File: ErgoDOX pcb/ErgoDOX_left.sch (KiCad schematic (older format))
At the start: 105 parts, among them J1 AudioJack4, J2 USB_B_Micro, SW0:10 SW0:3, SW0:11 SW0:2, SW0:12 SW0:1, SW0:7 SW0:6, SW0:8 SW0:5, SW0:9 SW0:4, SW1 TS-1187A-B-A-B, SW1:10 SW1:3, SW1:11 SW1:2, SW1:12 SW1:1, SW1:13 SW1:0, SW1:9 SW1:4, SW2:10 SW2:3, SW2:11 SW2:2, SW2:12 SW2:1, SW2:13 SW2:0, SW2:7 SW2:6, SW2:8 SW2:5, SW2:9 SW2:4, SW3:10 SW3:3, SW3:11 SW3:2, SW3:12 SW3:1, SW3:13 SW3:0, SW3:8 SW3:5, SW3:9 SW3:4, SW4:10 SW4:3, SW4:11 SW4:2, SW4:12 SW4:1, SW4:13 SW4:0, SW4:7 SW4:6, SW4:8 SW4:5, SW4:9 SW4:4, SW5:10 SW5:3, SW5:11 SW5:2, SW5:12 SW5:1, SW5:13 SW5:0, SW5:7 SW5:6, SW5:8 SW5:5, SW5:9 SW5:4, U1 ATmega32U4-MU, U2 MCP23018, Y1 16MHz

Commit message: finished LH routing
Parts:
- removed R6, R7: 1k, Resistors_SMD:R_0603, symbol Device:R_US
- removed U2: MCP23018, Housings_SSOP:SSOP-24_5.3x8.2mm_Pitch0.65mm, symbol ErgoDOX:MCP23018
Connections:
- no-connect marks 12 -> 6
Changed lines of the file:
@@
 	1    0    0    -1
 $EndComp
-Text Label 14400 4200 0    60   ~ 0
-COL1
 Text Label 13300 1450 2    60   ~ 0
 LED_A
@@
 	1    0    0    -1
 $EndComp
-Text Label 14400 5100 0    60   ~ 0
-ROW4
-Text Label 14400 5200 0    60   ~ 0
-ROW3
-Text Label 14400 5300 0    60   ~ 0
-ROW2
-Text Label 14400 5400 0    60   ~ 0
-ROW1
-Text Label 14400 5500 0    60   ~ 0
-ROW0
-Text Label 14400 4700 0    60   ~ 0
-COL6
-Text Label 14400 4600 0    60   ~ 0
-COL5
-Text Label 14400 4100 0    60   ~ 0
-COL0
-Text Label 14400 4300 0    60   ~ 0
-COL2
-Text Label 14400 4400 0    60   ~ 0
-COL3
-Text Label 14400 4500 0    60   ~ 0
-COL4
-Text Label 12400 4350 0    60   ~ 0
-SCL
-Text Label 12400 4450 0    60   ~ 0
-SDA
-NoConn ~ 12800 5500
-NoConn ~ 12800 4950
-NoConn ~ 12800 4850
 $Comp
 L ErgoDOX:SWITCH_PUSH SW2:10
@@
 	1    0    0    -1
 $EndComp
-Text Label 14400 5000 0    60   ~ 0
-ROW5
 Text Label 1300 5800 2    60   ~ 0
 ROW5
@@
 	1    0    0    -1
 $EndComp
-NoConn ~ 14400 4800
 $Comp
 L ErgoDOX:SWITCH_PUSH SW1:9
@@
 	1    0    0    -1
 $EndComp
-NoConn ~ 12800 5600
-NoConn ~ 12800 5700
 Text Label 5200 9550 3    60   ~ 0
 COL12
@@
 Wire Wire Line
 	2200 6900 2200 6700
-Wire Wire Line
-	12350 4200 12350 4350
-Wire Wire Line
-	12250 4200 12250 4450
 Connection ~ 2300 8400
 Wire Wire Line
@@
 Connection ~ 4400 9050
 Connection ~ 3000 9050
-Text Label 14400 5600 0    60   ~ 0
-LED_B
-Text Label 14400 5700 0    60   ~ 0
-LED_A
 Wire Wire Line
 	2300 8400 3000 8400
@@
 $EndComp
 $Comp
-L Device:R_US R7
-U 1 1 5F7D2D04
-P 12350 4050
-F 0 "R7" H 12418 4096 50  0000 L CNN
-F 1 "1k" H 12418 4005 50  0000 L CNN
-F 2 "Resistors_SMD:R_0603" V 12390 4040 50  0001 C CNN
-F 3 "~" H 12350 4050 50  0001 C CNN
-	1    12350 4050
-	1    0    0    -1
-$EndComp
-$Comp
-L Device:R_US R6
-U 1 1 5F7D30B0
-P 12250 4050
-F 0 "R6" H 12182 4004 50  0000 R CNN
-F 1 "1k" H 12182 4095 50  0000 R CNN
-F 2 "Resistors_SMD:R_0603" V 12290 4040 50  0001 C CNN
-F 3 "~" H 12250 4050 50  0001 C CNN
-	1    12250 4050
-	1    0    0    1
-$EndComp
-$Comp
-L power:VCC #PWR0110
-U 1 1 5F7D3AAF
-P 12300 3900
-F 0 "#PWR0110" H 12300 3750 50  0001 C CNN
-F 1 "VCC" H 12315 4073 50  0000 C CNN
-F 2 "" H 12300 3900 50  0001 C CNN
-F 3 "" H 12300 3900 50  0001 C CNN
-	1    12300 3900
-	1    0    0    -1
-$EndComp
-Wire Wire Line
-	12250 3900 12300 3900
-Connection ~ 12300 3900
-Wire Wire Line
-	12300 3900 12350 3900
-$Comp
 L power:GND #PWR0111
 U 1 1 5F7E762D
@@
 Wire Wire Line
 	14000 3100 13950 3100
-$Comp
-L power:GND #PWR0114
-U 1 1 5F857BF3
-P 12800 4650
-F 0 "#PWR0114" H 12800 4400 50  0001 C CNN
-F 1 "GND" V 12805 4522 50  0000 R CNN
-F 2 "" H 12800 4650 50  0001 C CNN
-F 3 "" H 12800 4650 50  0001 C CNN
-	1    12800 4650
-	0    1    1    0
-$EndComp
-$Comp
-L power:VCC #PWR0115
-U 1 1 5F858643
-P 12800 4100
-F 0 "#PWR0115" H 12800 3950 50  0001 C CNN
-F 1 "VCC" H 12815 4273 50  0000 C CNN
-F 2 "" H 12800 4100 50  0001 C CNN
-F 3 "" H 12800 4100 50  0001 C CNN
-	1    12800 4100
-	1    0    0    -1
-$EndComp
-$Comp
-L ErgoDOX:MCP23018 U2
-U 1 1 5F78DF8E
-P 13600 4900
-F 0 "U2" H 13600 6048 60  0000 C CNN
-F 1 "MCP23018" H 13600 5942 60  0000 C CNN
-F 2 "Housings_SSOP:SSOP-24_5.3x8.2mm_Pitch0.65mm" H 13600 4900 50  0001 C CNN
-F 3 "" H 13600 4900 50  0001 C CNN
-	1    13600 4900
-	1    0    0    -1
-$EndComp
 $Comp
 L Switch:SW_Push SW1
@@
 Text Label 13450 2250 2    60   ~ 0
 SDA
-Wire Wire Line
-	12250 4450 12800 4450
-Wire Wire Line
-	12350 4350 12800 4350
 Text Label 9950 2150 2    60   ~ 0
 RST

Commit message: USB breakout draft
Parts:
- added J101: USB_C_Receptacle_USB2.0, Connectors_USB:USB_C_Receptacle_Amphenol_12401548E4-2A, symbol Connector:USB_C_Receptacle_USB2.0
- added J102: USB_B_Mini, ErgoDOX:CUI_UJ2-MABH-1-SMT, symbol Connector:USB_B_Mini
- added J2, J201, J202, J203: USB_B, ErgoDOX:usb_breakout, symbol Connector:USB_B
- J103: renamed from J2; Purchase (none) -> https://www.digikey.com/en/products/detail/amphenol-icc-fci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
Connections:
- net GND: now also J101.A1 (GND), J101.A12 (GND), J101.B1 (GND), J101.B12 (GND), J101.S1 (SHIELD), J102.5 (GND), J102.6 (Shield), J2.4 (GND), J2.5 (Shield), J201.4 (GND), J201.5 (Shield), J202.4 (GND), J202.5 (Shield), J203.4 (GND), J203.5 (Shield)
- net USB+: now also J2.3 (D+); no longer J103.3 (D+)
- net USB-: now also J2.2 (D-); no longer J103.2 (D-)
- net VCC: now also J2.1 (VBUS); no longer J103.1 (VBUS)
- new net: J101.A4 (VBUS), J101.A9 (VBUS), J101.B4 (VBUS), J101.B9 (VBUS), J201.1 (VBUS)
- new net: J101.A6 (D+), J101.B6 (D+), J201.3 (D+)
- new net: J101.A7 (D-), J101.B7 (D-), J201.2 (D-)
- new net: J102.1 (VBUS), J202.1 (VBUS)
- new net: J102.2 (D-), J202.2 (D-)
- new net: J102.3 (D+), J202.3 (D+)
- new net: J103.1 (VBUS), J203.1 (VBUS)
- new net: J103.2 (D-), J203.2 (D-)
- new net: J103.3 (D+), J203.3 (D+)
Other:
- moved on the sheet: J103
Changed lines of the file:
@@
 	10550 1750 10550 1850
 $Comp
-L Connector:USB_B_Micro J2
+L Connector:USB_B_Micro J103
 U 1 1 6007DBC8
+P 3550 4700
+F 0 "J103" H 3607 5167 50  0000 C CNN
+F 1 "USB_B_Micro" H 3607 5076 50  0000 C CNN
+F 2 "Connectors_USB:USB_Micro-B_Wuerth-629105150521" H 3700 4650 50  0001 C CNN
+F 3 "~" H 3700 4650 50  0001 C CNN
+F 4 "https://www.digikey.com/en/products/detail/amphenol-icc-fci/10118193-0001LF/2785388" H 3550 4700 50  0001 C CNN "Purchase"
+	1    3550 4700
+	1    0    0    -1
+$EndComp
+$Comp
+L Connector:USB_B_Mini J102
+U 1 1 5FA03103
+P 3550 3550
+F 0 "J102" H 3607 4017 50  0000 C CNN
+F 1 "USB_B_Mini" H 3607 3926 50  0000 C CNN
+F 2 "ErgoDOX:CUI_UJ2-MABH-1-SMT" H 3700 3500 50  0001 C CNN
+F 3 "~" H 3700 3500 50  0001 C CNN
+F 4 "https://www.digikey.com/en/products/detail/cui-devices/UJ2-MABH-1-SMT-TR/6187919" H 3550 3550 50  0001 C CNN "Purchase"
+	1    3550 3550
+	1    0    0    -1
+$EndComp
+$Comp
+L Connector:USB_B J2
+U 1 1 5FA06E9E
 P 8850 3150
 F 0 "J2" H 8907 3617 50  0000 C CNN
-F 1 "USB_B_Micro" H 8907 3526 50  0000 C CNN
-F 2 "Connectors_USB:USB_Micro-B_Wuerth-629105150521" H 9000 3100 50  0001 C CNN
-F 3 "~" H 9000 3100 50  0001 C CNN
+F 1 "USB_B" H 8907 3526 50  0000 C CNN
+F 2 "ErgoDOX:usb_breakout" H 9000 3100 50  0001 C CNN
+F 3 " ~" H 9000 3100 50  0001 C CNN
 	1    8850 3150
 	1    0    0    -1
 $EndComp
+$Comp
+L Connector:USB_B J201
+U 1 1 5FA08FDF
+P 4700 2000
+F 0 "J201" H 4470 1989 50  0000 R CNN
+F 1 "USB_B" H 4470 1898 50  0000 R CNN
+F 2 "ErgoDOX:usb_breakout" H 4850 1950 50  0001 C CNN
+F 3 " ~" H 4850 1950 50  0001 C CNN
+	1    4700 2000
+	-1   0    0    -1
+$EndComp
+$Comp
+L Connector:USB_B J202
+U 1 1 5FA09CCE
+P 4500 3550
+F 0 "J202" H 4270 3539 50  0000 R CNN
+F 1 "USB_B" H 4270 3448 50  0000 R CNN
+F 2 "ErgoDOX:usb_breakout" H 4650 3500 50  0001 C CNN
+F 3 " ~" H 4650 3500 50  0001 C CNN
+	1    4500 3550
+	-1   0    0    -1
+$EndComp
+$Comp
+L Connector:USB_B J203
+U 1 1 5FA0A566
+P 4500 4700
+F 0 "J203" H 4270 4689 50  0000 R CNN
+F 1 "USB_B" H 4270 4598 50  0000 R CNN
+F 2 "ErgoDOX:usb_breakout" H 4650 4650 50  0001 C CNN
+F 3 " ~" H 4650 4650 50  0001 C CNN
+	1    4500 4700
+	-1   0    0    -1
+$EndComp
+Wire Wire Line
+	3850 4500 4200 4500
+Wire Wire Line
+	4200 4700 3850 4700
+Wire Wire Line
+	3850 4800 4200 4800
+$Comp
+L power:GND #PWR0110
+U 1 1 5FA40674
+P 4000 5100
+F 0 "#PWR0110" H 4000 4850 50  0001 C CNN
+F 1 "GND" H 4005 4927 50  0000 C CNN
+F 2 "" H 4000 5100 50  0001 C CNN
+F 3 "" H 4000 5100 50  0001 C CNN
+	1    4000 5100
+	1    0    0    -1
+$EndComp
+Wire Wire Line
+	3450 5100 3550 5100
+Connection ~ 3550 5100
+Wire Wire Line
+	3550 5100 4000 5100
+Wire Wire Line
+	4500 5100 4600 5100
+Connection ~ 4500 5100
+Connection ~ 4000 5100
+Wire Wire Line
+	4000 5100 4500 5100
+Wire Wire Line
+	3450 3950 3550 3950
+Connection ~ 3550 3950
+Wire Wire Line
+	3550 3950 4050 3950
+Connection ~ 4500 3950
+Wire Wire Line
+	4500 3950 4600 3950
+$Comp
+L power:GND #PWR0114
+U 1 1 5FA8801B
+P 4050 3950
+F 0 "#PWR0114" H 4050 3700 50  0001 C CNN
+F 1 "GND" H 4055 3777 50  0000 C CNN
+F 2 "" H 4050 3950 50  0001 C CNN
+F 3 "" H 4050 3950 50  0001 C CNN
+	1    4050 3950
+	1    0    0    -1
+$EndComp
+Connection ~ 4050 3950
+Wire Wire Line
+	4050 3950 4500 3950
+Wire Wire Line
+	3850 3550 4200 3550
+Wire Wire Line
+	4200 3650 3850 3650
+Wire Wire Line
+	3850 3350 4200 3350
+Wire Wire Line
+	3950 2100 4050 2100
+Wire Wire Line
+	4050 2100 4050 2000
+Wire Wire Line
+	4050 2000 3950 2000
+Wire Wire Line
+	4050 2000 4400 2000
+Connection ~ 4050 2000
+Wire Wire Line
+	4400 2100 4250 2100
+Wire Wire Line
+	4250 2100 4250 1800
+Wire Wire Line
+	4250 1800 4050 1800
+Wire Wire Line
+	3950 1900 4050 1900
+Wire Wire Line
+	4050 1900 4050 1800
+Connection ~ 4050 1800
+Wire Wire Line
+	4050 1800 3950 1800
+Wire Wire Line
+	4400 1800 4400 1300
+Wire Wire Line
+	4400 1300 3950 1300
+$Comp
+L power:GND #PWR0115
+U 1 1 5FB25F7C
+P 4750 2450
+F 0 "#PWR0115" H 4750 2200 50  0001 C CNN
+F 1 "GND" H 4755 2277 50  0000 C CNN
+F 2 "" H 4750 2450 50  0001 C CNN
+F 3 "" H 4750 2450 50  0001 C CNN
+	1    4750 2450
+	1    0    0    -1
+$EndComp
+Wire Wire Line
+	4700 2400 4750 2400
+Wire Wire Line
+	4750 2450 4750 2400
+Connection ~ 4750 2400
+Wire Wire Line
+	4750 2400 4800 2400
+$Comp
+L power:GND #PWR0118
+U 1 1 5FB4F6CF
+P 3200 2850
+F 0 "#PWR0118" H 3200 2600 50  0001 C CNN
+F 1 "GND" H 3205 2677 50  0000 C CNN
+F 2 "" H 3200 2850 50  0001 C CNN
+F 3 "" H 3200 2850 50  0001 C CNN
+	1    3200 2850
+	1    0    0    -1
+$EndComp
+Wire Wire Line
+	3050 2800 3200 2800
+Wire Wire Line
+	3200 2850 3200 2800
+Connection ~ 3200 2800
+Wire Wire Line
+	3200 2800 3350 2800
+$Comp
+L Connector:USB_C_Receptacle_USB2.0 J101
+U 1 1 5FA00F68
+P 3350 1900
+F 0 "J101" H 3457 2767 50  0000 C CNN
+F 1 "USB_C_Receptacle_USB2.0" H 3457 2676 50  0000 C CNN
+F 2 "Connectors_USB:USB_C_Receptacle_Amphenol_12401548E4-2A" H 3500 1900 50  0001 C CNN
+F 3 "https://www.usb.org/sites/default/files/documents/usb_type-c.zip" H 3500 1900 50  0001 C CNN
+F 4 "https://www.digikey.com/en/products/detail/gct/USB4110-GF-A/10384547" H 3350 1900 50  0001 C CNN "Purchase"
+	1    3350 1900
+	1    0    0    -1
+$EndComp

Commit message: Updated USB footprints
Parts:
- J101: footprint Connectors_USB:USB_C_Receptacle_Amphenol_12401548E4-2A -> ErgoDOX:USB4110-GF-A
- J103: footprint Connectors_USB:USB_Micro-B_Wuerth-629105150521 -> ErgoDOX:10118193-0001LF
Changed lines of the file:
@@
 F 0 "J103" H 3607 5167 50  0000 C CNN
 F 1 "USB_B_Micro" H 3607 5076 50  0000 C CNN
-F 2 "Connectors_USB:USB_Micro-B_Wuerth-629105150521" H 3700 4650 50  0001 C CNN
+F 2 "ErgoDOX:10118193-0001LF" H 3700 4650 50  0001 C CNN
 F 3 "~" H 3700 4650 50  0001 C CNN
 F 4 "https://www.digikey.com/en/products/detail/amphenol-icc-fci/10118193-0001LF/2785388" H 3550 4700 50  0001 C CNN "Purchase"
@@
 F 0 "J101" H 3457 2767 50  0000 C CNN
 F 1 "USB_C_Receptacle_USB2.0" H 3457 2676 50  0000 C CNN
-F 2 "Connectors_USB:USB_C_Receptacle_Amphenol_12401548E4-2A" H 3500 1900 50  0001 C CNN
+F 2 "ErgoDOX:USB4110-GF-A" H 3500 1900 50  0001 C CNN
 F 3 "https://www.usb.org/sites/default/files/documents/usb_type-c.zip" H 3500 1900 50  0001 C CNN
 F 4 "https://www.digikey.com/en/products/detail/gct/USB4110-GF-A/10384547" H 3350 1900 50  0001 C CNN "Purchase"

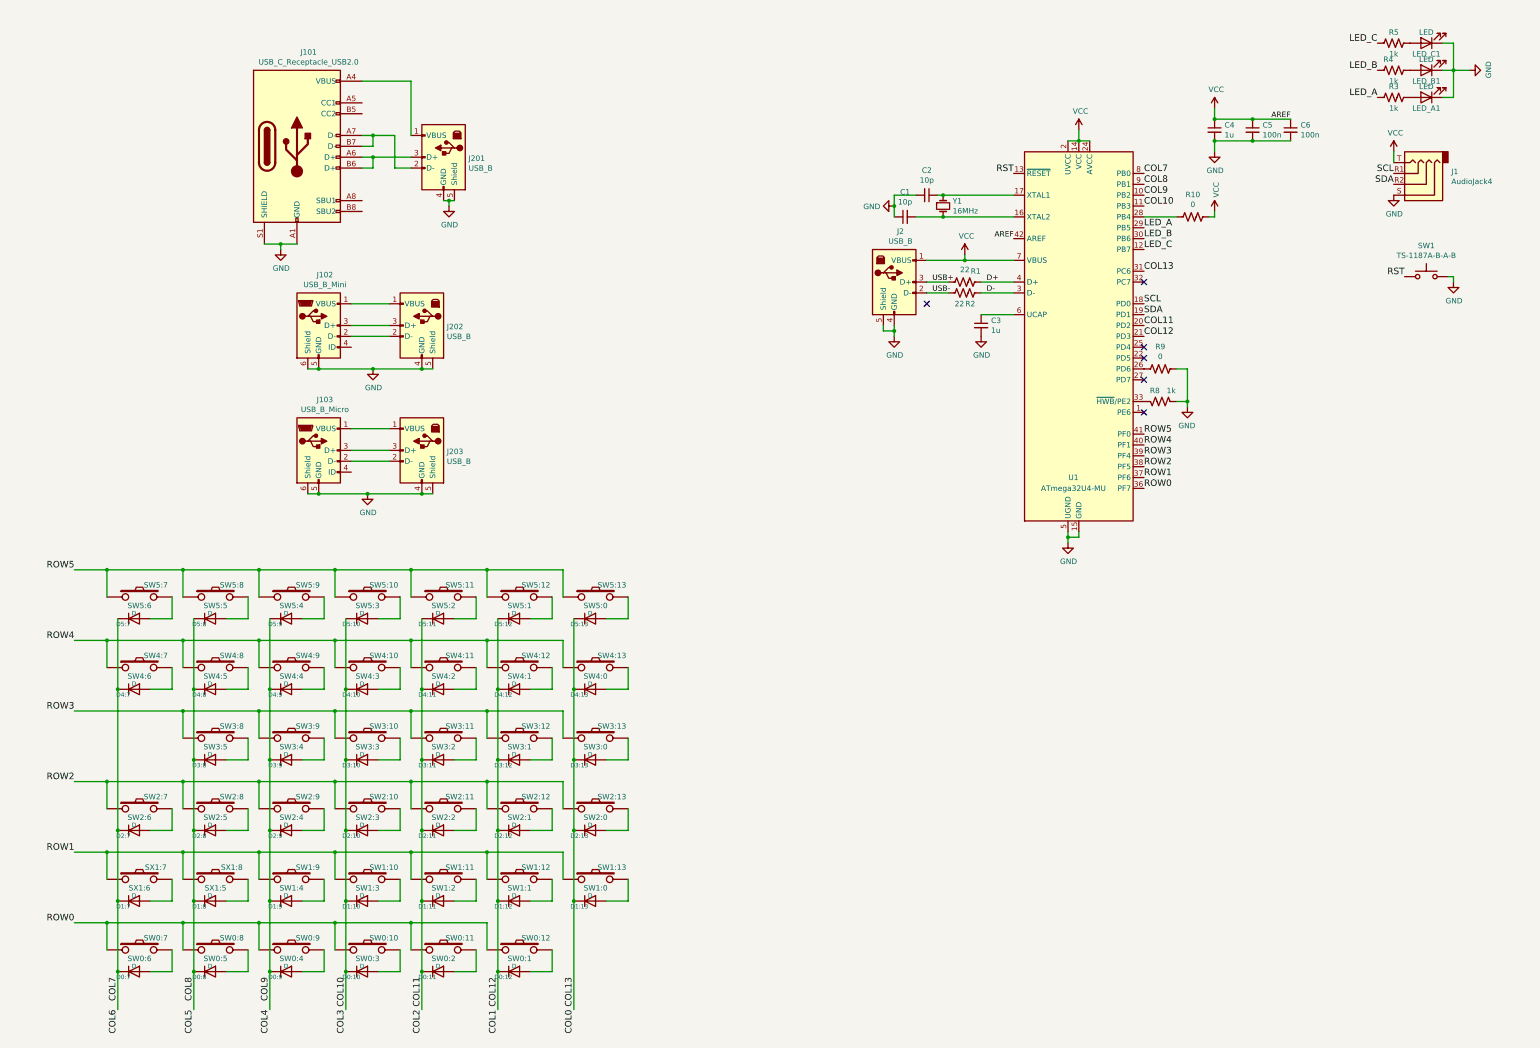
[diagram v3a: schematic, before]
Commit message: Added revision, generated gerbers
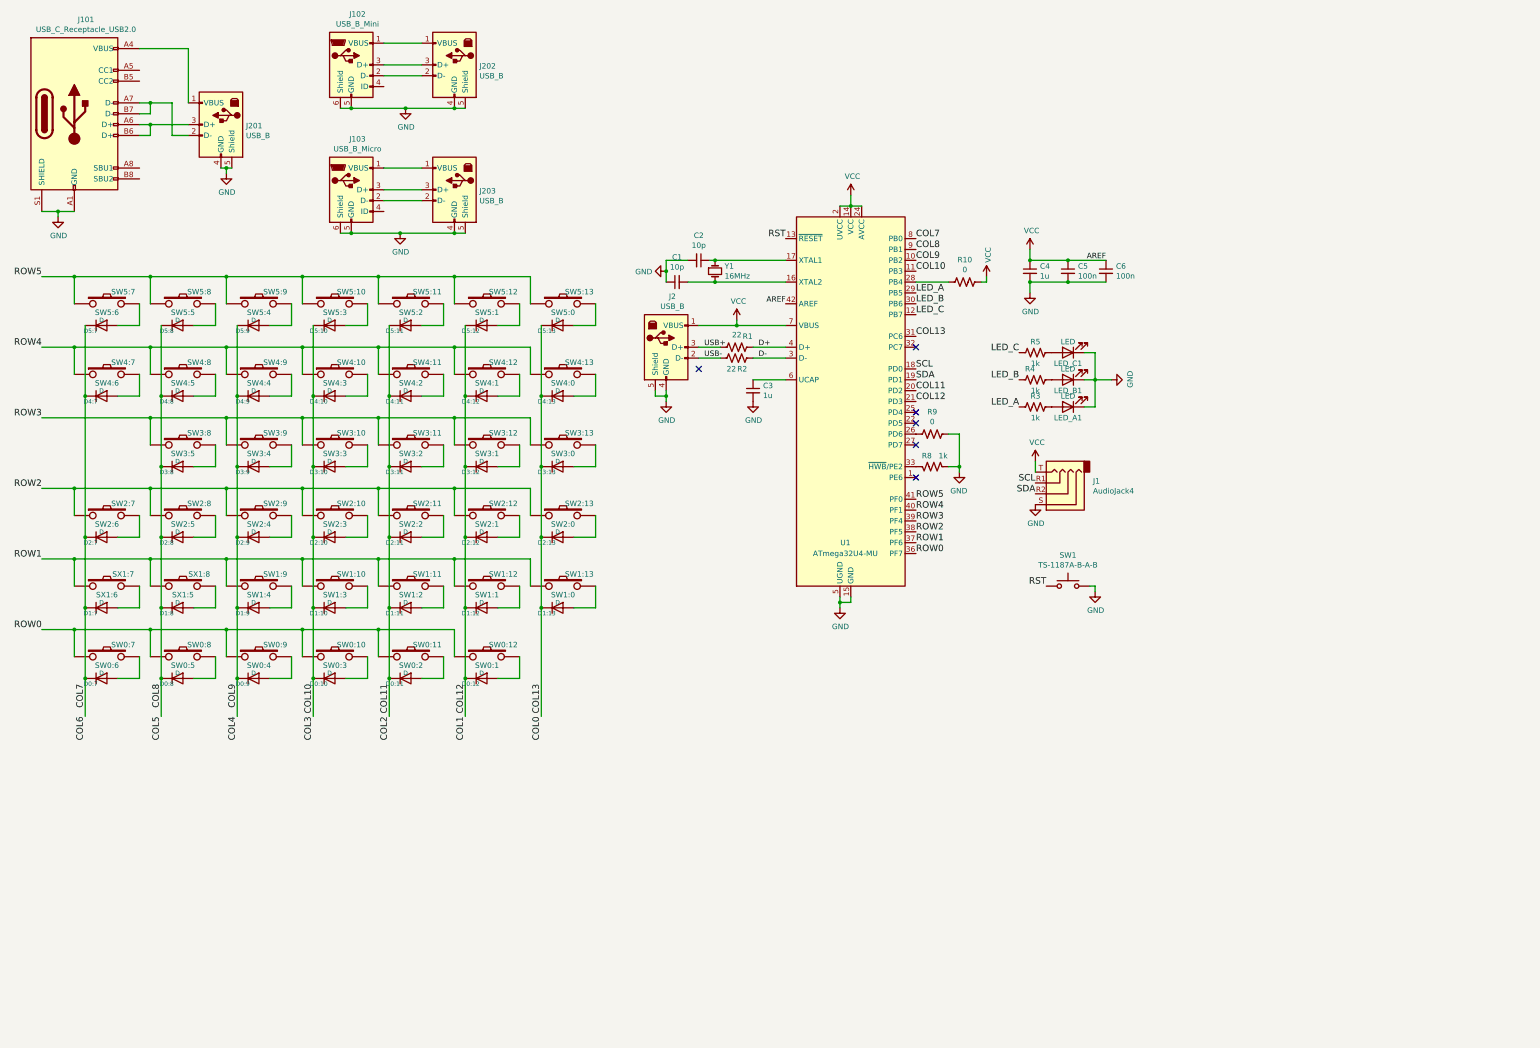
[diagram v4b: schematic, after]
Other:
- moved on the sheet: C1, C2, C3, C4, C5, C6, D0:10, D0:11, D0:12, D0:7, D0:8, D0:9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
